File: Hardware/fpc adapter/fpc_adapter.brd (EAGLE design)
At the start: 35 x 35 mm, 15 parts, among them X2 52746-20

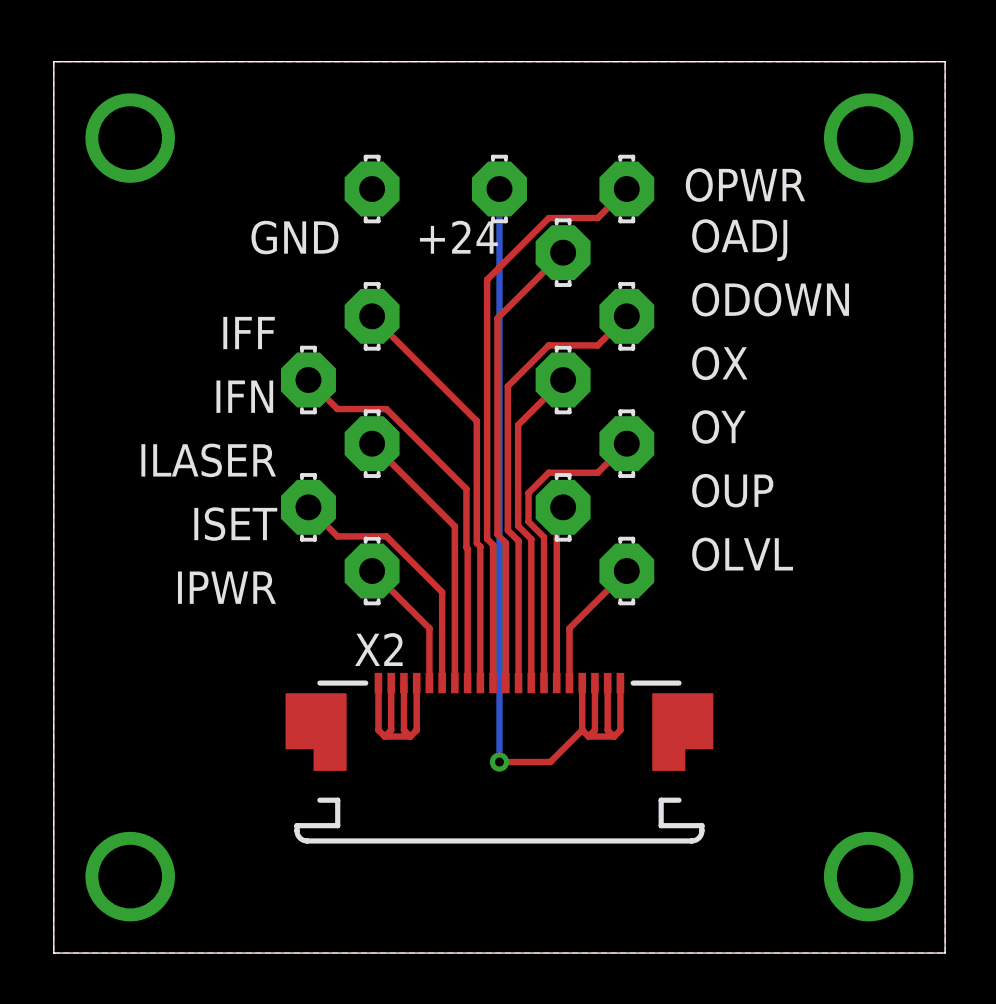
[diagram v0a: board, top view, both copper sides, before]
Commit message: сделал плату более узкой,чтоб она помещалась в дырку под разъем
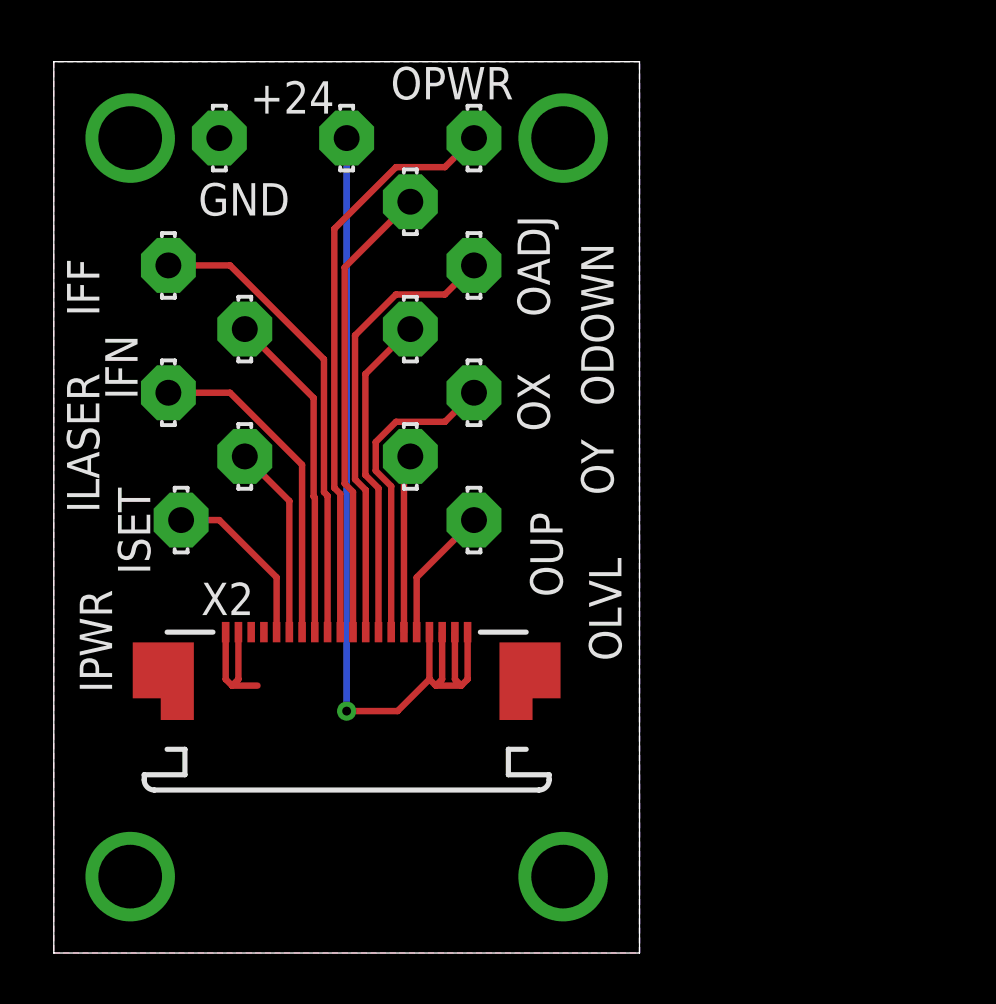
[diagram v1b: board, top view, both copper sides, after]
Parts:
- moved IFF 8.25 mm to (4.50, 27.0)
- moved ILASER 8.25 mm to (4.50, 22.0)
- moved IPWR 7.76 mm to (5.00, 17.0)
- moved +24 6.32 mm to (11.5, 32.0)
- moved GND 6.32 mm to (6.50, 32.0)
- moved OADJ 6.32 mm to (14.0, 29.5)
- moved ODOWN 6.32 mm to (16.5, 27.0)
- moved OLVL 6.32 mm to (16.5, 17.0)
- moved OPWR 6.32 mm to (16.5, 32.0)
- moved OUP 6.32 mm to (14.0, 19.5)
- moved OX 6.32 mm to (14.0, 24.5)
- moved OY 6.32 mm to (16.5, 22.0)
- moved X2 6.32 mm to (11.5, 12.0)
- moved IFN 3.20 mm to (7.50, 24.5)
- moved ISET 3.20 mm to (7.50, 19.5)
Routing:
- net GND: track 9.81 -> 5.41 mm
- net SET_SIG: track 10.2 -> 7.62 mm
- net FN_SIG: track 15.6 -> 13.0 mm
- net LASER_SIG: track 10.7 -> 13.0 mm
- net FF_SIG: track 16.2 -> 18.4 mm
- net PRW_SIG: track 5.33 -> 6.83 mm
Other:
- board size 35 x 35 mm -> 23 x 35 mm

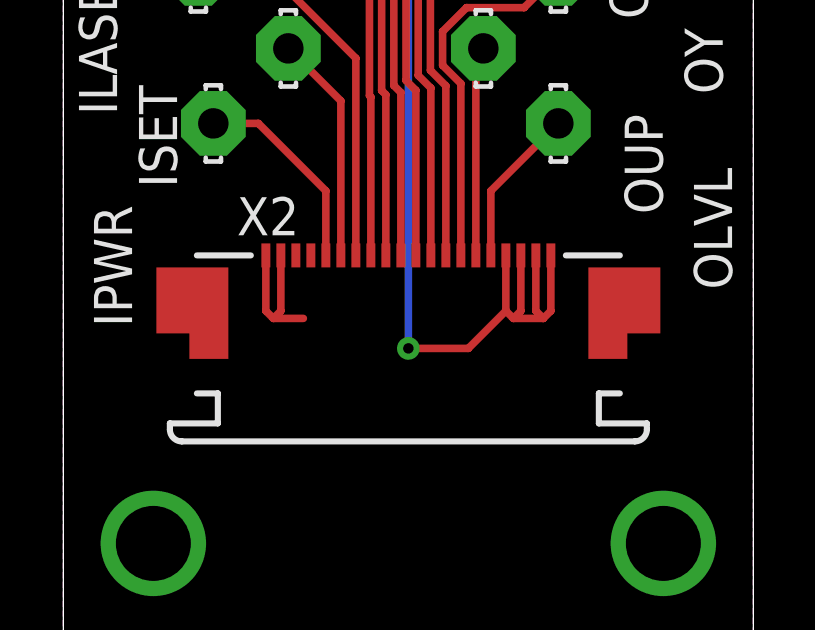
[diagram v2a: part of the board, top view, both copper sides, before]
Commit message: по требованию с производства увеличил зазорполигона до 0,2мм на обеих платах. заказ переделал. заказе указал покрытие ПОС 63 вместо имерсионного олова
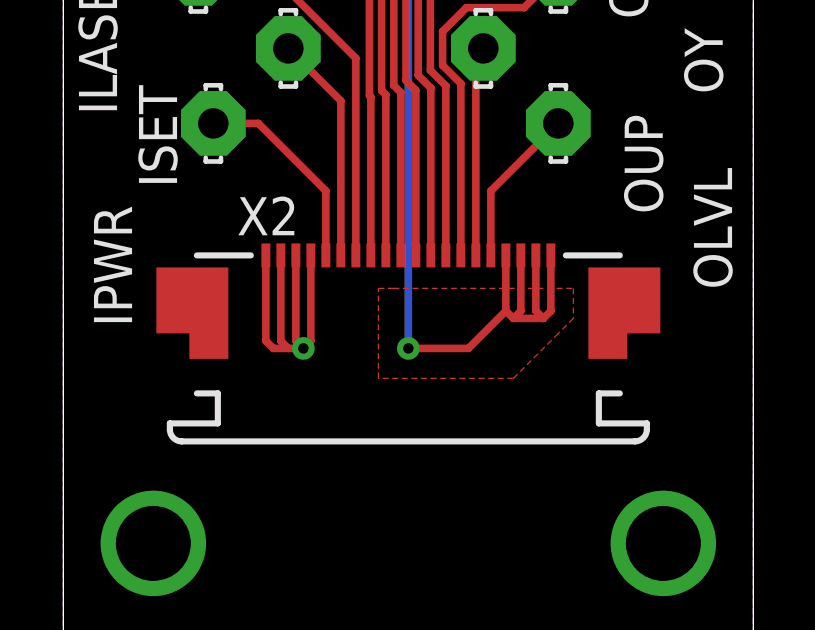
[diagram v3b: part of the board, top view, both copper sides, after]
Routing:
- net GND: track 5.41 -> 13.8 mm, vias 4 -> 5
- added copper zone on layer 1, net +24V
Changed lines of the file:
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@@
 </class>
 </classes>
-<designrules name="default">
+<designrules name="default *">
 <description language="de">&lt;b&gt;EAGLE Design Rules&lt;/b&gt;
 &lt;p&gt;
@@
 <param name="srMinRoundness" value="0mil"/>
 <param name="srMaxRoundness" value="0mil"/>
-<param name="slThermalIsolate" value="10mil"/>
+<param name="slThermalIsolate" value="20mil"/>
 <param name="slThermalsForVias" value="0"/>
 <param name="dpMaxLengthDifference" value="10mm"/>
@@
 <contactref element="X2" pad="4"/>
 <contactref element="GND" pad="MP"/>
-<wire x1="6.75" y1="12.6" x2="6.75" y2="10.75" width="0.254" layer="1"/>
-<wire x1="6.75" y1="10.75" x2="7" y2="10.5" width="0.254" layer="1"/>
-<wire x1="7" y1="10.5" x2="8" y2="10.5" width="0.254" layer="1"/>
-<wire x1="7.25" y1="12.6" x2="7.25" y2="10.75" width="0.254" layer="1"/>
-<wire x1="7.25" y1="10.75" x2="7" y2="10.5" width="0.254" layer="1"/>
 <via x="3" y="32" extent="1-16" drill="2.5"/>
 <via x="3" y="3" extent="1-16" drill="2.5"/>
 <via x="20" y="32" extent="1-16" drill="2.5"/>
 <via x="20" y="3" extent="1-16" drill="2.5"/>
-<polygon width="0.254" layer="16">
+<polygon width="0.254" layer="16" isolate="0.254">
 <vertex x="0" y="35"/>
 <vertex x="0" y="0"/>
@@
 <vertex x="23" y="35"/>
 </polygon>
-<polygon width="0.254" layer="1">
+<polygon width="0.254" layer="1" isolate="0.254" rank="2">
 <vertex x="0" y="35"/>
 <vertex x="0" y="0"/>
@@
 <vertex x="23" y="35"/>
 </polygon>
+<via x="8" y="9.5" extent="1-16" drill="0.35"/>
+<wire x1="8.25" y1="12.6" x2="8.25" y2="9.75" width="0.254" layer="1"/>
+<wire x1="8.25" y1="9.75" x2="8" y2="9.5" width="0.254" layer="1"/>
+<wire x1="7.75" y1="12.6" x2="7.75" y2="9.75" width="0.254" layer="1"/>
+<wire x1="7.75" y1="9.75" x2="8" y2="9.5" width="0.254" layer="1"/>
+<wire x1="8" y1="9.5" x2="7.5" y2="9.5" width="0.254" layer="1"/>
+<wire x1="7.5" y1="9.5" x2="7" y2="9.5" width="0.254" layer="1"/>
+<wire x1="7" y1="9.5" x2="6.75" y2="9.75" width="0.254" layer="1"/>
+<wire x1="6.75" y1="9.75" x2="6.75" y2="12.6" width="0.254" layer="1"/>
+<wire x1="7.25" y1="12.6" x2="7.25" y2="9.75" width="0.254" layer="1"/>
+<wire x1="7.25" y1="9.75" x2="7.5" y2="9.5" width="0.254" layer="1"/>
 </signal>
 <signal name="+24V">
@@
 <via x="11.5" y="9.5" extent="1-16" drill="0.35"/>
 <wire x1="11.5" y1="9.5" x2="11.5" y2="32" width="0.254" layer="16"/>
+<polygon width="0.1524" layer="1" isolate="0.254">
+<vertex x="11" y="11.5"/>
+<vertex x="17" y="11.5"/>
+<vertex x="17" y="10.5"/>
+<vertex x="16.5" y="10"/>
+<vertex x="15" y="8.5"/>
+<vertex x="10.5" y="8.5"/>
+<vertex x="10.5" y="11.5"/>
+</polygon>
 </signal>
 <signal name="PRW_SIG">
